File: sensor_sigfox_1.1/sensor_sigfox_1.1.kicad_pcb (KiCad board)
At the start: 2 copper layers, 27.8 x 60.1 mm, 38 parts, among them IC1 AS5600-ASOM, IC2 WSSFM11R2DAT, J1 UDPI, J2 Battery, J4 Conn_Coaxial, Q1 DMC2053UVT, U1 MLX90393, U2 ATtiny826-X, U3 MT3608, Y1 Crystal

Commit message: iniciar conexiones a nuevos comps
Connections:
- C3 pad 2: Net-(C1-Pad2) -> +5V
- C5 pad 1: Net-(C1-Pad2) -> Net-(C5-Pad1)
- C6 pad 1: Net-(C1-Pad2) -> Net-(C5-Pad1)
- C8 pad 1: unconnected-(C8-Pad1) -> GND
- C8 pad 2: unconnected-(C8-Pad2) -> Net-(U2-Pad8)
- C9 pad 1: unconnected-(C9-Pad1) -> GND
- C9 pad 2: unconnected-(C9-Pad2) -> Net-(U2-Pad9)
- D2 pad 1: Net-(C1-Pad2) -> +5V
- IC1 pad 1: Net-(C1-Pad2) -> Net-(C5-Pad1)
- IC1 pad 2: Net-(C1-Pad2) -> Net-(C5-Pad1)
- IC1 pad 5: Net-(U2-Pad8) -> unconnected-(IC1-Pad5)
- IC1 pad 6: Net-(R5-Pad1) -> unconnected-(IC1-Pad6)
- IC1 pad 7: Net-(R4-Pad1) -> unconnected-(IC1-Pad7)
- IC1 pad 8: Net-(C1-Pad2) -> Net-(C5-Pad1)
- R10 pad 2: Net-(C1-Pad2) -> +5V
- R4 pad 1: Net-(R4-Pad1) -> /SCL
- R5 pad 1: Net-(R5-Pad1) -> /SDA
- R8 pad 1: Net-(R8-Pad1) -> unconnected-(R8-Pad1)
- U1 pad 10: unconnected-(U1-Pad10) -> GND
- U1 pad 13: unconnected-(U1-Pad13) -> GND
- U1 pad 14: unconnected-(U1-Pad14) -> GND
- U1 pad 16: unconnected-(U1-Pad16) -> GND
- U1 pad 17: unconnected-(U1-Pad17) -> GND
- U1 pad 3: unconnected-(U1-Pad3) -> /SCL
- U1 pad 4: unconnected-(U1-Pad4) -> GND
- U1 pad 5: unconnected-(U1-Pad5) -> /SDA
- U1 pad 8: unconnected-(U1-Pad8) -> VCC
- U1 pad 9: unconnected-(U1-Pad9) -> GND
- U2 pad 10: Net-(R5-Pad1) -> /SDA
- U2 pad 11: Net-(R4-Pad1) -> /SCL
- U2 pad 7: Net-(R8-Pad1) -> unconnected-(U2-Pad7)
- U2 pad 9: unconnected-(U2-Pad9) -> Net-(U2-Pad9)
- Y1 pad 1: unconnected-(Y1-Pad1) -> Net-(U2-Pad8)
- Y1 pad 2: unconnected-(Y1-Pad2) -> Net-(U2-Pad9)
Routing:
- net Net-(C5-Pad1): track 0.00 -> 76.4 mm, vias 0 -> 4
- net Net-(C1-Pad2): track 76.4 -> 0.00 mm, vias 4 -> 0
- net Net-(R4-Pad1): track 50.1 -> 0.00 mm
- net /SCL: track 0.00 -> 50.1 mm
- net Net-(R5-Pad1): track 49.0 -> 0.00 mm, vias 2 -> 0
- net /SDA: track 0.00 -> 49.0 mm, vias 0 -> 2
- net unconnected-(R8-Pad1): track 0.00 -> 4.39 mm
- net Net-(R8-Pad1): track 4.39 -> 0.00 mm

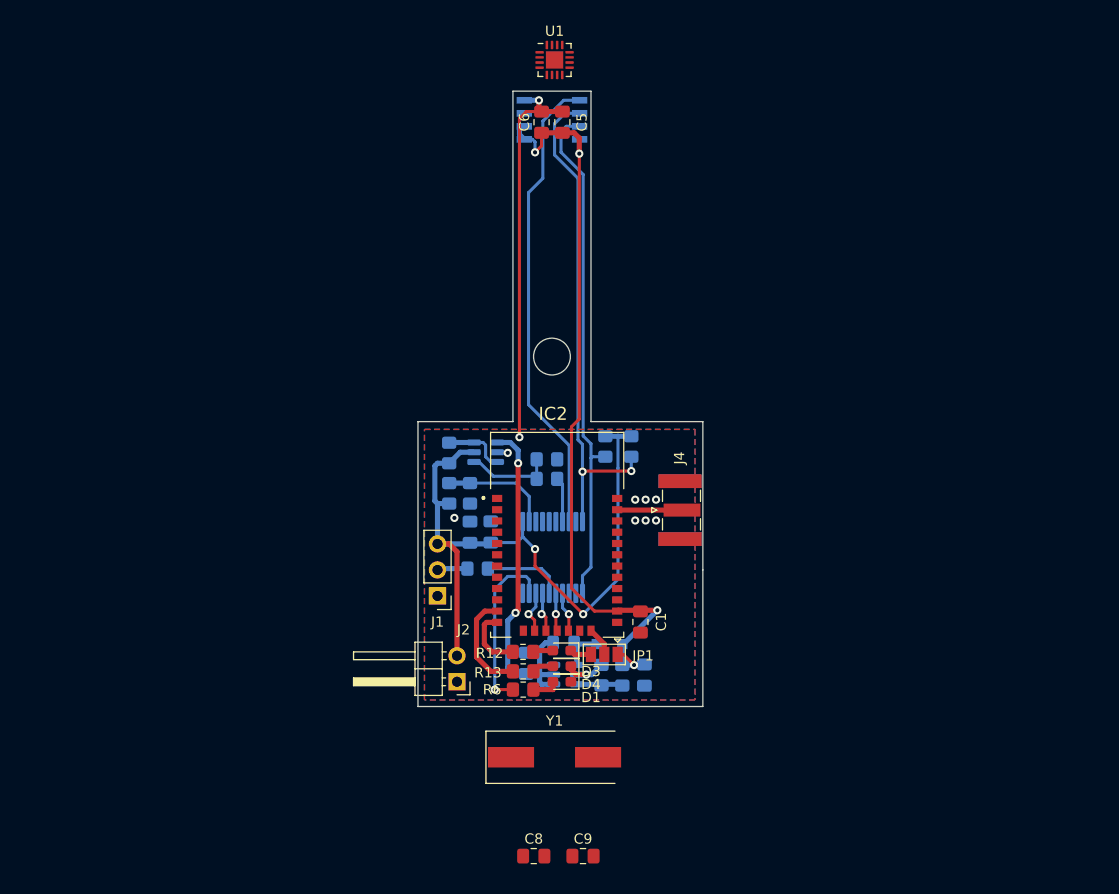
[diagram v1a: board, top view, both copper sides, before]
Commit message: componentes borrados
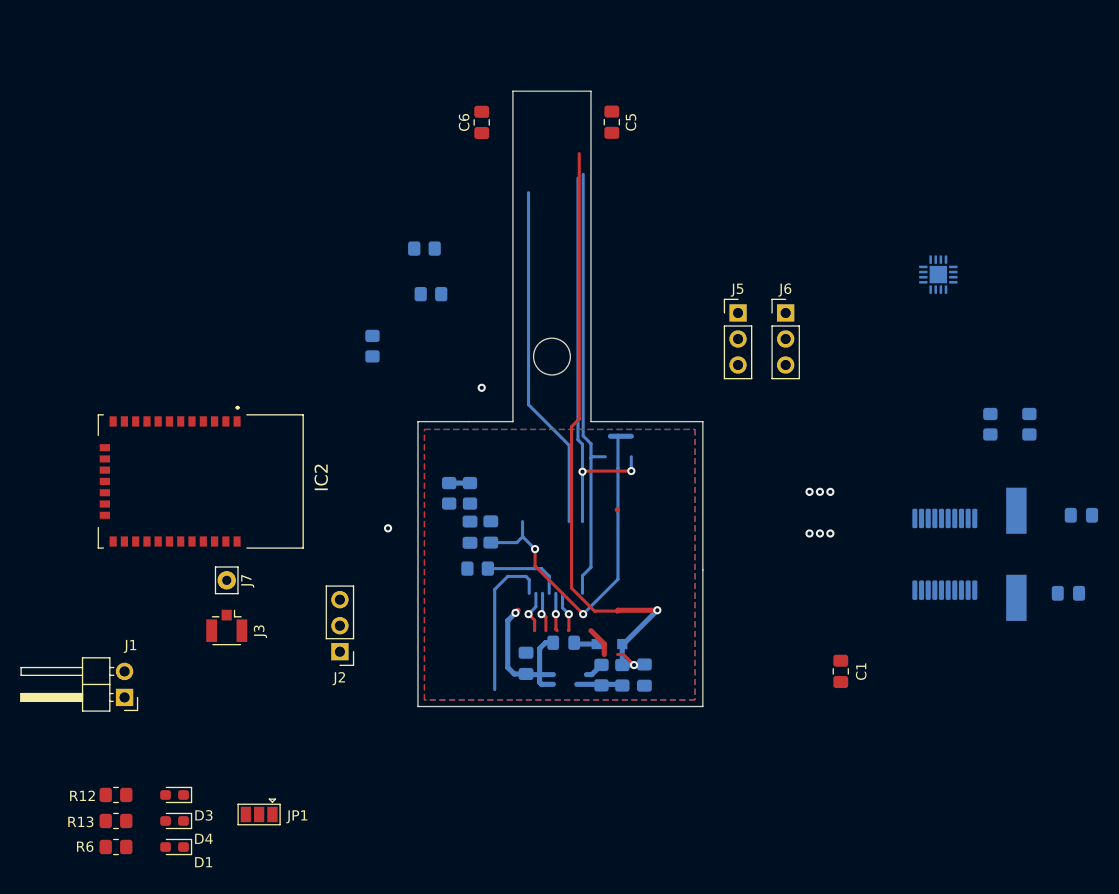
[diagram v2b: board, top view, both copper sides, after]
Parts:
- removed IC1: AS5600-ASOM, AS5600-ASOM:SOIC127P600X175-8N
- removed J4: Conn_Coaxial, Connector_Coaxial:SMA_Samtec_SMA-J-P-X-ST-EM1_EdgeMount
- removed Q1: DMC2053UVT, Package_TO_SOT_SMD:TSOT-23-6
- removed U3: MT3608, Package_TO_SOT_SMD:SOT-23-6
- added J3: Antenna, Connector_Coaxial:U.FL_Hirose_U.FL-R-SMT-1_Vertical, F.Cu at (95.0, 88.3)
- added J5: I2C, Connector_PinHeader_2.54mm:PinHeader_1x03_P2.54mm_Vertical, F.Cu at (144.9, 57.7)
- added J6: UART, Connector_PinHeader_2.54mm:PinHeader_1x03_P2.54mm_Vertical, F.Cu at (149.6, 57.7)
- added J7: Conn_01x01_Female, Connector_Pin:Pin_D0.9mm_L10.0mm_W2.4mm_FlatFork, F.Cu at (95.0, 83.8)
- C8, C9, U1: moved to B.Cu
- Y1: value Crystal -> 32.768 kHz; moved to B.Cu
- moved C9 58.9 mm to (178.4, 77.5), turned to 180 degrees
- moved C8 58.2 mm to (177.2, 85.1), turned to 180 degrees
- moved Y1 49.2 mm to (172.1, 81.3), turned to 90 degrees
- moved U1 42.9 mm to (164.5, 54.0), turned to 180 degrees
- moved R6 42.6 mm to (84.2, 109.9)
- moved R13 42.3 mm to (84.2, 107.3)
- moved R12 42.1 mm to (84.2, 104.8)
- moved D1 41.1 mm to (89.9, 109.9)
- moved D4 40.7 mm to (89.9, 107.3)
- moved D3 40.3 mm to (89.9, 104.8)
- moved R5 38.9 mm to (173.4, 68.6)
- moved U2 38.3 mm to (165.1, 81.3)
- moved R4 37.7 mm to (169.5, 68.6)
- moved JP1 37.1 mm to (98.2, 106.7)
- moved IC2 35.2 mm to (92.5, 74.2), turned to -90 degrees
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- renumbered J2 to J1, J1 to J2
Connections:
- net Net-(U2-Pad17) renamed /SF_RX
- net Net-(U2-Pad18) renamed /SF_TX
- IC2 pad 10: unconnected-(IC2-Pad10) -> Net-(IC2-Pad10)
- IC2 pad 11: Net-(IC2-Pad11) -> unconnected-(IC2-Pad11)
- IC2 pad 12: Net-(IC2-Pad12) -> unconnected-(IC2-Pad12)
- IC2 pad 16: Net-(U2-Pad15) -> unconnected-(IC2-Pad16)
- IC2 pad 17: Net-(IC2-Pad17) -> unconnected-(IC2-Pad17)
- IC2 pad 31: GND -> unconnected-(IC2-Pad31)
- JP1 pad 1: Net-(C1-Pad2) -> unconnected-(JP1-Pad1)
- JP1 pad 3: GND -> unconnected-(JP1-Pad3)
- R13 pad 1: Net-(IC2-Pad11) -> Net-(IC2-Pad10)
- U1 pad 15: unconnected-(U1-Pad15) -> VCC
- U2 pad 14: Net-(IC2-Pad17) -> unconnected-(U2-Pad14)
- U2 pad 15: Net-(U2-Pad15) -> unconnected-(U2-Pad15)
- U2 pad 19: Net-(R6-Pad1) -> unconnected-(U2-Pad19)
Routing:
- net Net-(C5-Pad1): track 76.4 -> 0.00 mm, vias 4 -> 0
- net +5V: track 0.00 -> 63.1 mm, vias 0 -> 2
- net GND: track 45.2 -> 1.87 mm, vias 11 -> 8
- net VCC: track 66.5 -> 35.8 mm
- net Net-(C7-Pad2): track 35.0 -> 17.1 mm, vias 2 -> 1
- net (no net): track 0.00 -> 15.7 mm
- net Net-(C8-Pad2): track 45.8 -> 33.8 mm
- net Net-(IC2-Pad11): track 10.2 -> 0.00 mm
- net /SDA: track 49.0 -> 39.9 mm
- net Net-(R2-Pad1): track 10.8 -> 2.03 mm
- net Net-(Q1-Pad1): track 8.71 -> 0.00 mm
- net /SCL: track 50.1 -> 43.0 mm
- net Net-(IC2-Pad12): track 6.34 -> 0.00 mm
- net Net-(IC2-Pad30): track 6.35 -> 0.05 mm
- net Net-(Q1-Pad3): track 6.17 -> 0.00 mm
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
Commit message: wip pcb new
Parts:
- removed the C3 at (135.8, 93.1)
- removed the C4 at (120.8, 79.1)
- removed C7: 22u, Capacitor_SMD:C_0805_2012Metric_Pad1.18x1.45mm_HandSolder
- removed D2: SD103, Diode_SMD:D_SOD-323_HandSoldering
- removed D3, D4: LED_Small, LED_SMD:LED_0603_1608Metric_Pad1.05x0.95mm_HandSolder
- removed J5: I2C, Connector_PinHeader_2.54mm:PinHeader_1x03_P2.54mm_Vertical
- removed J6: UART, Connector_PinHeader_2.54mm:PinHeader_1x03_P2.54mm_Vertical
- removed JP1: Jumper_3_Open, Jumper:SolderJumper-3_P1.3mm_Open_Pad1.0x1.5mm
- removed L1: 4.7u, Inductor_SMD:L_0805_2012Metric_Pad1.15x1.40mm_HandSolder
- removed R10, R7: 10k, Resistor_SMD:R_0805_2012Metric_Pad1.20x1.40mm_HandSolder
- removed R11: 2k, Resistor_SMD:R_0805_2012Metric_Pad1.20x1.40mm_HandSolder
- removed R12, R13, R6: 330, Resistor_SMD:R_0805_2012Metric_Pad1.20x1.40mm_HandSolder
- removed R5: 2.2k, Resistor_SMD:R_0805_2012Metric_Pad1.20x1.40mm_HandSolder
- removed R8: 470, Resistor_SMD:R_0805_2012Metric_Pad1.20x1.40mm_HandSolder
- removed R9: 100k, Resistor_SMD:R_0805_2012Metric_Pad1.20x1.40mm_HandSolder
- C1: value 100n -> 10u; moved to B.Cu
- C5: moved to B.Cu
- C6: value 10u -> 100n; moved to B.Cu
- J1: footprint Connector_PinHeader_2.54mm:PinHeader_1x02_P2.54mm_Horizontal -> Battery:BatteryHolder_Keystone_2468_2xAAA; moved to B.Cu
- J2: value UDPI -> Conn_01x07_Socket; footprint Connector_PinHeader_2.54mm:PinHeader_1x03_P2.54mm_Vertical -> Connector_PinHeader_2.54mm:PinHeader_1x07_P2.54mm_Vertical; moved to B.Cu
- J3: value Antenna -> Conn_01x01_Female; footprint Connector_Coaxial:U.FL_Hirose_U.FL-R-SMT-1_Vertical -> Connector_Pin:Pin_D0.9mm_L10.0mm_W2.4mm_FlatFork
- J4: renamed from J7; value Conn_01x01_Female -> Antenna; footprint Connector_Pin:Pin_D0.9mm_L10.0mm_W2.4mm_FlatFork -> Connector_Coaxial:U.FL_Hirose_U.FL-R-SMT-1_Vertical
- R2: value 220k -> 2.2k
- R3: value 100k -> 2.2k
- R4: value 2.2k -> 330; moved to F.Cu
- moved D1 86.1 mm to (137.7, 38.3), turned to 0 degrees
- moved C3 54.5 mm to (123.0, 79.2), turned to 90 degrees
- moved C6 49.5 mm to (124.0, 88.4), turned to 180 degrees
- moved J3 45.4 mm to (140.0, 94.7), turned to 0 degrees
- moved C4 45.4 mm to (133.1, 79.2), turned to 90 degrees
- moved Y1 44.3 mm to (128.3, 74.4), turned to 0 degrees
- moved R4 41.7 mm to (137.7, 41.6), turned to 0 degrees
- moved J4 41.2 mm to (135.0, 93.8), turned to -90 degrees
- moved IC1 39.9 mm to (131.0, 84.4)
- moved U1 37.1 mm to (128.0, 82.0)
- moved C1 33.3 mm to (123.0, 83.1)
- moved U2 31.0 mm to (137.7, 38.3)
- moved J1 30.9 mm to (114.9, 87.5), turned to 0 degrees
- moved R3 17.9 mm to (128.1, 90.5), turned to 180 degrees
- moved R2 17.5 mm to (128.1, 88.5), turned to 180 degrees
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- renumbered C8 to C3, C9 to C4, IC2 to IC1, U2 to U1, U1 to U2
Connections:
- C1 pad 2: Net-(C1-Pad2) -> VCC
- C5 pad 1: Net-(C5-Pad1) -> GND
- C5 pad 2: GND -> Net-(U1-PA4)
- C6 pad 1: Net-(C5-Pad1) -> GND
- C6 pad 2: GND -> Net-(IC1-VDD_IO)
- D1 pad 2: Net-(D1-Pad2) -> Net-(D1-A)
- IC1 pad 10: Net-(IC2-Pad10) -> Net-(IC1-GPIO4)
- IC1 pad 19: Net-(IC2-Pad19) -> Net-(IC1-RST_N)
- IC1 pad 21: Net-(C1-Pad2) -> Net-(IC1-VDD_IO)
- IC1 pad 31: unconnected-(IC2-Pad31) -> GND
- J2 pad 2: Net-(J2-Pad2) -> VCC
- J2 pad 3: VCC -> Net-(J2-Pin_3)
- R1 pad 2: Net-(J2-Pad2) -> Net-(J2-Pin_3)
- R2 pad 1: Net-(R2-Pad1) -> /SCL
- R3 pad 1: GND -> /SDA
- R3 pad 2: Net-(R2-Pad1) -> VCC
- R4 pad 1: /SCL -> Net-(IC1-GPIO4)
- R4 pad 2: VCC -> Net-(D1-A)
- U1 pad 2: unconnected-(U2-Pad2) -> Net-(U1-PA4)
- U1 pad 4: unconnected-(U2-Pad4) -> Net-(IC1-RST_N)
- U2 pad 15: VCC -> Net-(U1-PA4)
- U2 pad 8: VCC -> Net-(U1-PA4)
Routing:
- net +5V: track 63.1 -> 0.00 mm, vias 2 -> 0
- net /SCL: track 43.0 -> 0.00 mm
- net /SDA: track 39.9 -> 0.00 mm, vias 2 -> 0
- net VCC: track 35.8 -> 0.00 mm, vias 2 -> 0
- net Net-(U1-PB3): track 33.8 -> 0.00 mm
- net Net-(C7-Pad2): track 17.1 -> 0.00 mm, vias 1 -> 0
- net (no net): track 15.7 -> 0.00 mm
- net Net-(R6-Pad1): track 15.1 -> 0.00 mm
- net Net-(U1-~{RESET}/PA0): track 7.96 -> 0.00 mm
- net Net-(R10-Pad1): track 4.49 -> 0.00 mm
- net Net-(IC2-Pad19): track 2.86 -> 0.00 mm
- net Net-(D2-Pad2): track 2.61 -> 0.00 mm
- net Net-(R2-Pad1): track 2.03 -> 0.00 mm
- net GND: track 1.87 -> 0.00 mm, vias 8 -> 0
- net unconnected-(U1-PC3-Pad15): vias 1 -> 0
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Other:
- outline, holes or cut-outs redrawn

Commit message: wip
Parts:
- removed J1: Battery, Battery:BatteryHolder_Keystone_2468_2xAAA
- C1, C2, C3, C4, C5, C6, R1, R2, R3, U2: moved to F.Cu
- U1: footprint Package_SO:SSOP-20_5.3x7.2mm_P0.65mm -> Package_DFN_QFN:VQFN-20-1EP_3x3mm_P0.4mm_EP1.7x1.7mm; moved to F.Cu
- Y1: footprint Crystal:Crystal_SMD_HC49-SD -> Crystal:Crystal_C26-LF_D2.1mm_L6.5mm_Vertical; moved to F.Cu
- moved R3 40.7 mm to (137.8, 51.0), turned to 0 degrees
- moved R2 36.9 mm to (137.8, 53.0), turned to 0 degrees
- moved C4 17.4 mm to (117.6, 71.2)
- moved C2 14.0 mm to (130.7, 73.1)
- moved U1 12.2 mm to (135.7, 72.6), turned to 90 degrees
- moved Y1 11.3 mm to (139.6, 74.5), turned to 90 degrees
- moved C1 10.8 mm to (127.3, 73.2)
- moved C3 7.24 mm to (121.5, 72.2)
- moved D1 5.09 mm to (137.7, 43.4)
- moved R1 4.38 mm to (119.1, 91.5), turned to 0 degrees
- moved R4 3.53 mm to (137.7, 45.1)
- moved C6 3.32 mm to (122.9, 91.5), turned to 0 degrees
- moved IC1 1.09 mm to (130.9, 83.3)
- turned C5 to 0 degrees
- turned U2 to 0 degrees
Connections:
- C3 pad 2: Net-(U1-PB3) -> Net-(U1-PB0)
- U1 pad 1: VCC -> /SF_TX
- U1 pad 10: /SDA -> unconnected-(U1-PB4-Pad10)
- U1 pad 11: /SCL -> Net-(U1-PB0)
- U1 pad 12: unconnected-(U1-PC0-Pad12) -> Net-(U1-PB2)
- U1 pad 13: unconnected-(U1-PC1-Pad13) -> /SDA
- U1 pad 14: unconnected-(U1-PC2-Pad14) -> /SCL
- U1 pad 16: Net-(U1-~{RESET}/PA0) -> unconnected-(U1-PC1-Pad16)
- U1 pad 17: /SF_RX -> unconnected-(U1-PC2-Pad17)
- U1 pad 18: /SF_TX -> unconnected-(U1-PC3-Pad18)
- U1 pad 19: unconnected-(U1-PA3-Pad19) -> Net-(U1-~{RESET}/PA0)
- U1 pad 2: Net-(U1-PA4) -> unconnected-(U1-PA3-Pad2)
- U1 pad 20: GND -> /SF_RX
- U1 pad 3: unconnected-(U1-PA5-Pad3) -> GND
- U1 pad 4: Net-(IC1-RST_N) -> VCC
- U1 pad 5: unconnected-(U1-PA7-Pad5) -> Net-(U1-PA4)
- U1 pad 7: unconnected-(U1-PB4-Pad7) -> Net-(IC1-RST_N)
- U1 pad 8: Net-(U1-PB3) -> unconnected-(U1-PA7-Pad8)
- U1 pad 9: Net-(U1-PB2) -> unconnected-(U1-PB5-Pad9)
- Y1 pad 1: Net-(U1-PB3) -> Net-(U1-PB0)
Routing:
- net Net-(U1-~{RESET}/PA0): track 0.00 -> 28.6 mm
- net GND: track 0.00 -> 22.8 mm
- net /SF_RX: track 0.00 -> 22.2 mm
- net /SF_TX: track 0.00 -> 19.8 mm
- net /SDA: track 0.00 -> 12.1 mm
- net Net-(IC1-RF_IO): track 0.00 -> 10.0 mm
- net Net-(J2-Pin_3): track 0.00 -> 2.94 mm
- net Net-(IC1-VDD_IO): track 0.00 -> 2.55 mm
- net Net-(U1-PA4): track 0.00 -> 1.89 mm
- net Net-(D1-A): track 0.00 -> 1.76 mm

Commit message: wip almost ready
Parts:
- added J1: Battery, Battery:BatteryHolder_Keystone_2468_2xAAA, F.Cu at (115.9, 75.0)
- moved C4 23.0 mm to (140.3, 67.7), turned to -90 degrees
- moved C3 18.1 mm to (139.4, 74.4), turned to 180 degrees
- moved C1 4.69 mm to (132.0, 73.5), turned to -90 degrees
- moved Y1 2.25 mm to (139.4, 72.3)
- moved U1 1.37 mm to (135.3, 71.2), turned to 0 degrees
- moved C2 0.84 mm to (130.0, 73.5), turned to -90 degrees
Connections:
- C5 pad 2: Net-(U1-PA4) -> Net-(U1-PC3)
- U1 pad 18: unconnected-(U1-PC3-Pad18) -> Net-(U1-PC3)
- U1 pad 5: Net-(U1-PA4) -> unconnected-(U1-PA4-Pad5)
- U2 pad 15: Net-(U1-PA4) -> Net-(U1-PC3)
- U2 pad 8: Net-(U1-PA4) -> Net-(U1-PC3)
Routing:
- net GND: track 22.8 -> 124.2 mm, vias 0 -> 6
- net VCC: track 0.28 -> 98.7 mm, vias 0 -> 2
- net /SCL: track 0.00 -> 78.3 mm, vias 0 -> 1
- net /SDA: track 12.1 -> 79.4 mm, vias 0 -> 1
- net Net-(U1-PC3): track 0.00 -> 46.1 mm
- net Net-(IC1-GPIO4): track 0.00 -> 45.1 mm, vias 0 -> 4
- net /SF_TX: track 19.8 -> 43.6 mm, vias 0 -> 1
- net Net-(IC1-RST_N): track 0.00 -> 23.4 mm
- net /SF_RX: track 22.2 -> 43.4 mm, vias 0 -> 1
- net Net-(U1-~{RESET}/PA0): track 28.6 -> 37.0 mm
- net Net-(U1-PB3): track 0.00 -> 5.20 mm
- net Net-(U1-PB2): track 0.00 -> 5.16 mm
- net Net-(U1-PA4): track 1.89 -> 0.00 mm

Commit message: pcb wip
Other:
- board text added: "+"
- board text added: "C"
- board text added: "D"
- board text added: "GND"
- board text added: "P"
- board text added: "R"
- board text added: "T"

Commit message: sigfox
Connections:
- C6 pad 2: Net-(IC1-VDD_IO) -> VCC
- IC1 pad 21: Net-(IC1-VDD_IO) -> VCC
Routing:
- net GND: track 124.6 -> 172.3 mm
- net VCC: track 98.7 -> 125.1 mm, vias 2 -> 3
- net Net-(IC1-VDD_IO): track 2.55 -> 0.00 mm
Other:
- board text added: "-"
- board text removed: "GND"
